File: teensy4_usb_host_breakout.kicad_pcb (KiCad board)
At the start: 2 copper layers, 24.1 x 15.2 mm, 11 parts, among them J1 Conn_01x06, J2 USB_A, U1 TPD3S014

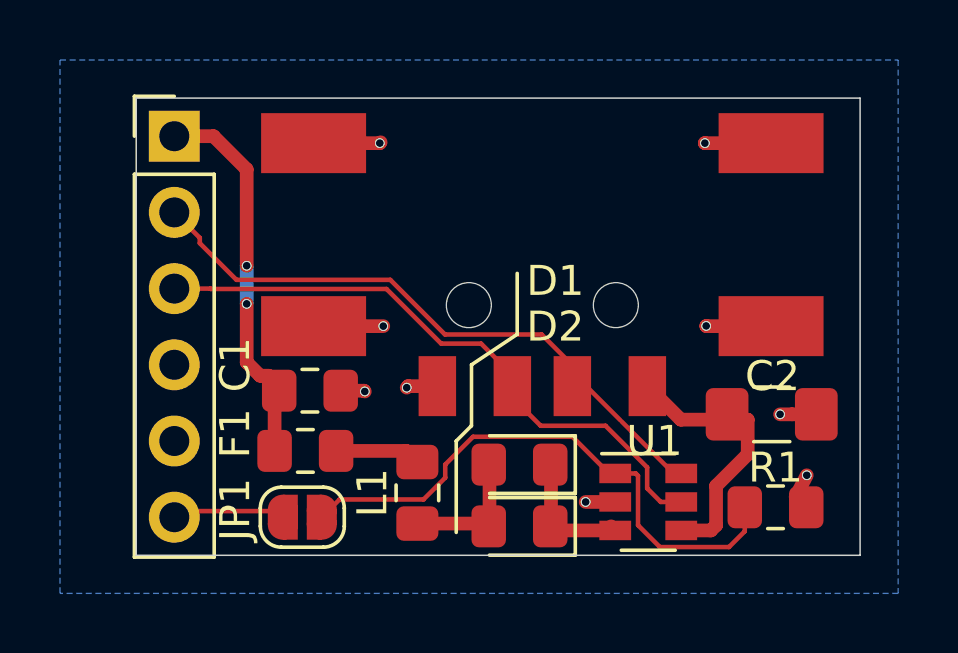
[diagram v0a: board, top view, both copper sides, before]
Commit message: Updated with Digikey part numbers. Removed diodes as TPD3S014DBVR provides reverse voltage protection
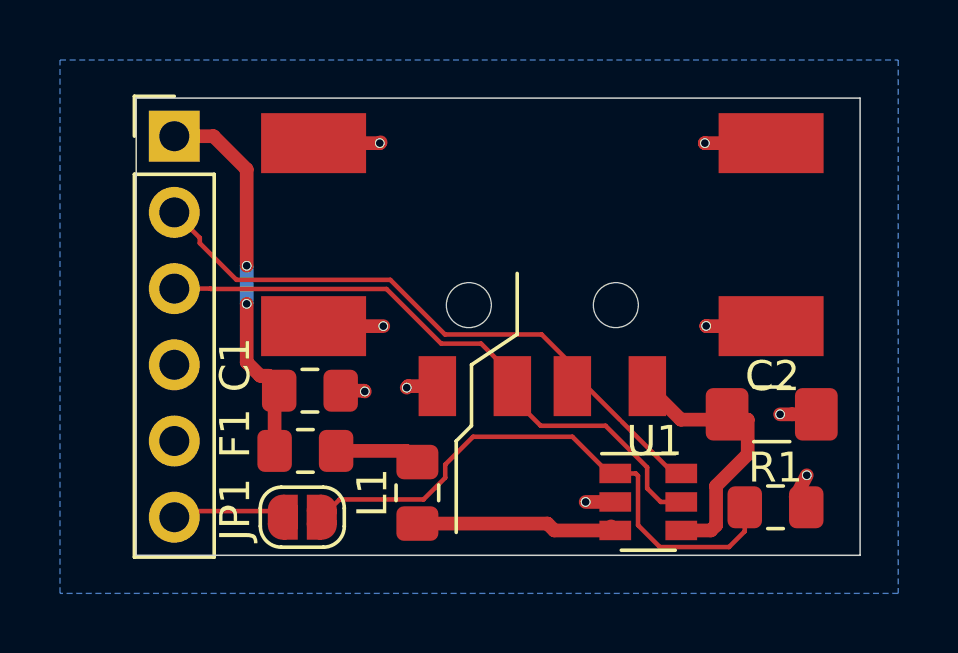
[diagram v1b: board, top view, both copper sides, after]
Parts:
- removed D1, D2: 1A, Diode_SMD:D_0805_2012Metric_Pad1.15x1.40mm_HandSolder
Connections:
- L1 pad 2: Net-(D1-Pad2) -> Net-(L1-Pad2)
- U1 pad 3: Net-(D1-Pad1) -> Net-(L1-Pad2)
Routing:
- net Net-(L1-Pad2): track 0.00 -> 6.89 mm
- net Net-(D1-Pad2): track 4.53 -> 0.00 mm
- net Net-(D1-Pad1): track 4.50 -> 0.00 mm

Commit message: Remove spurious silkscreen lines, update render
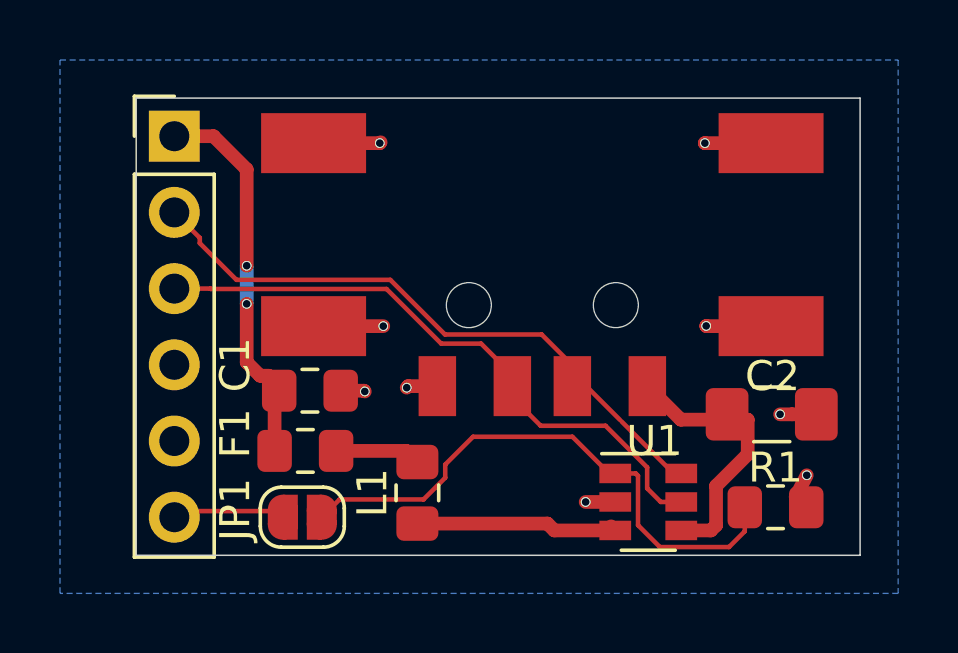
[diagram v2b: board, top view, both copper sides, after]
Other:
- board text added: "2019-09-22 Teensy 4.0 USB Host Breakout"
- board text removed: "2019-09-21 Teensy 4.0 USB Host Breakout"
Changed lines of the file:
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@@
   (general
     (thickness 1.6)
-    (drawings 16)
+    (drawings 11)
     (tracks 96)
     (zones 0)
@@
     )
   )
-  (gr_line (start 168.148 114.3) (end 168.148 117.348) (layer F.SilkS) (width 0.12))
-  (gr_line (start 168.656 113.792) (end 168.148 114.3) (layer F.SilkS) (width 0.12))
-  (gr_line (start 168.656 111.76) (end 168.656 113.792) (layer F.SilkS) (width 0.12))
-  (gr_line (start 170.18 110.744) (end 168.656 111.76) (layer F.SilkS) (width 0.12))
-  (gr_line (start 170.18 108.712) (end 170.18 110.744) (layer F.SilkS) (width 0.12))
-  (gr_text "2019-09-21\n\nTeensy 4.0\nUSB Host\nBreakout\n" (at 181.356 111.76) (layer B.SilkS)
+  (gr_text "2019-09-22\n\nTeensy 4.0\nUSB Host\nBreakout\n" (at 181.356 111.76) (layer B.SilkS)
     (effects (font (size 1.5 1.5) (thickness 0.3)) (justify left mirror))
   )

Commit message: Updated for jumper for enable (always on vs 27). Also updated docs
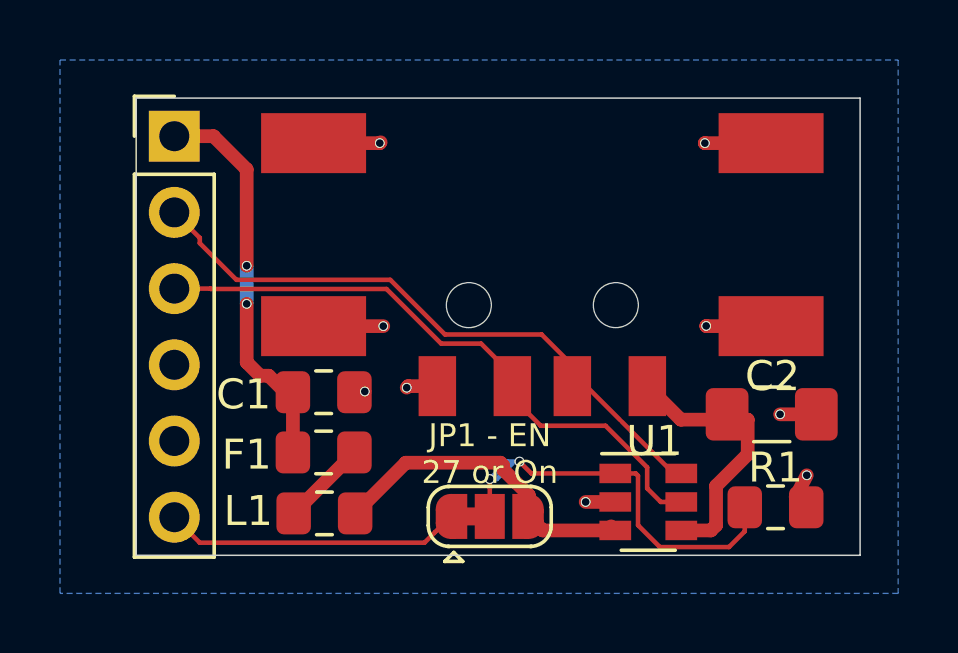
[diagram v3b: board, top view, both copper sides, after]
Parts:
- JP1: value EN -> EN PIN 27; footprint Jumper:SolderJumper-2_P1.3mm_Open_RoundedPad1.0x1.5mm -> Jumper:SolderJumper-3_P1.3mm_Bridged12_RoundedPad1.0x1.5mm
- moved JP1 6.25 mm to (169.3, 116.8)
- moved L1 3.17 mm to (163.8, 116.7), turned to 0 degrees
- moved F1 0.61 mm to (163.7, 114.7)
- moved C1 0.46 mm to (163.7, 112.7)
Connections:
- net Net-(JP1-Pad2) renamed /EN
- L1 pad 2: Net-(L1-Pad2) -> Net-(JP1-Pad3)
- U1 pad 3: Net-(L1-Pad2) -> Net-(JP1-Pad3)
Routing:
- net Net-(JP1-Pad3): track 0.00 -> 11.0 mm
- net Net-(L1-Pad2): track 6.89 -> 0.00 mm
- net /27: track 3.73 -> 10.2 mm
- net /EN: track 19.0 -> 14.3 mm, vias 0 -> 2
- net GND: track 14.5 -> 13.5 mm
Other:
- board text added: "2019-10-05 Teensy 4.0 USB Host Breakout"
- board text added: "JP1 - EN 27 or On"
- board text removed: "2019-09-22 Teensy 4.0 USB Host Breakout"
